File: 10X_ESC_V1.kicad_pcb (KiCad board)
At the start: 4 copper layers, 66 x 61.8 mm, 98 parts, among them J1 Conn_01x05_MountingPin, Q1 BUK7Y1R4-40H, Q2 BUK7Y1R4-40H, Q3 BUK7Y1R4-40H, Q4 BUK7Y1R4-40H, Q5 BUK7Y1R4-40H, Q7 BUK7Y1R4-40H, U1 STM32F051K8Ux, U2 DRV8300DPWR, U3 TPS62932, U4 TPS62932, U5 INA180B2

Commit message: D1~D3 부트스트랩 다이오드 제거 (DRV8300D 내장)
README에 있던 불필요한 다이오드 제거 완료
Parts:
- removed ?: , 
- removed D1, D2, D3: D, Diode_SMD:D_SMA
- removed REF**: Capacitor_Through_Hole, Footprints:Capacitor_Through_Hole
- TP6: value SWDIO -> TELEMRX
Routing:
- net +12V: track 74.0 -> 56.6 mm
- net Net-(U2-BSTC): track 6.15 -> 2.99 mm
- net Net-(U2-BSTB): track 5.42 -> 2.46 mm
- net Net-(U2-BSTA): track 5.25 -> 2.52 mm

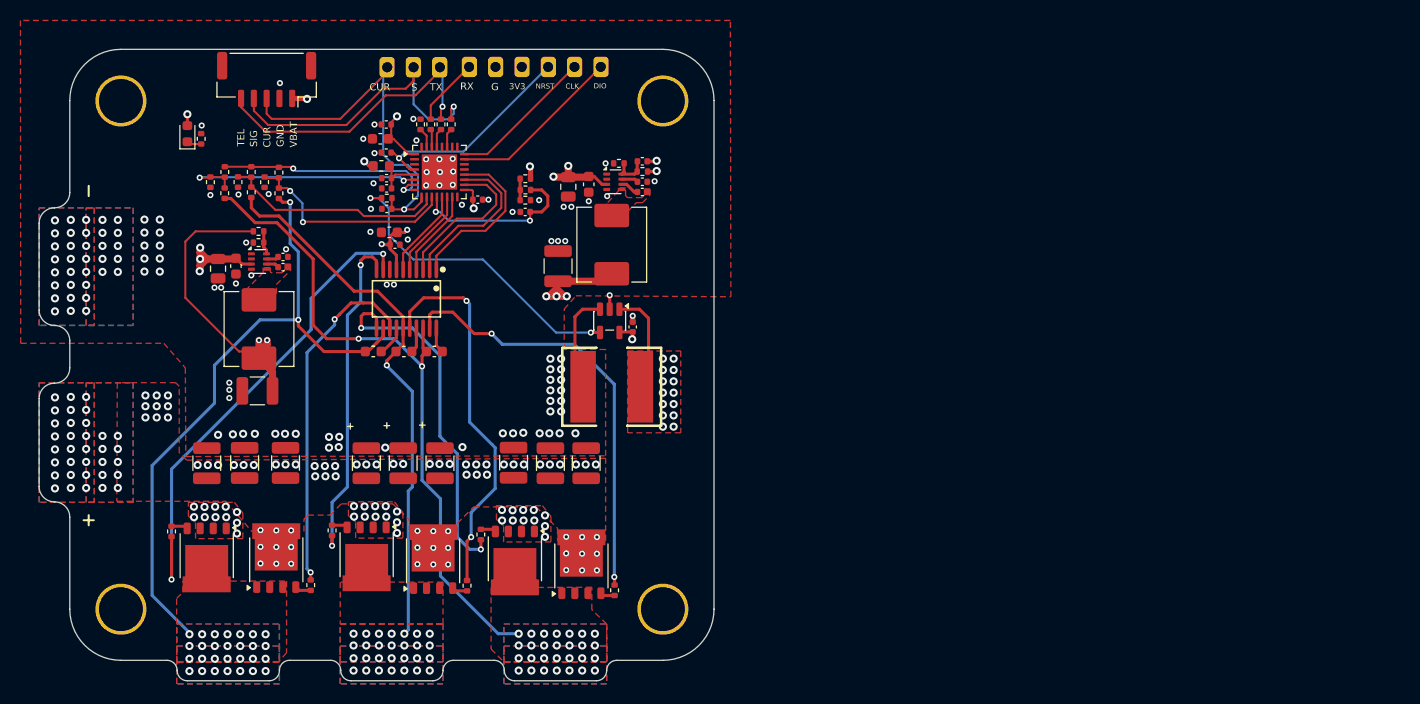
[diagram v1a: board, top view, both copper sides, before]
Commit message: V2 배치 연습
V2 배치 연습: 30x21 외곽선, MOSFET 아랫면 3열 배치
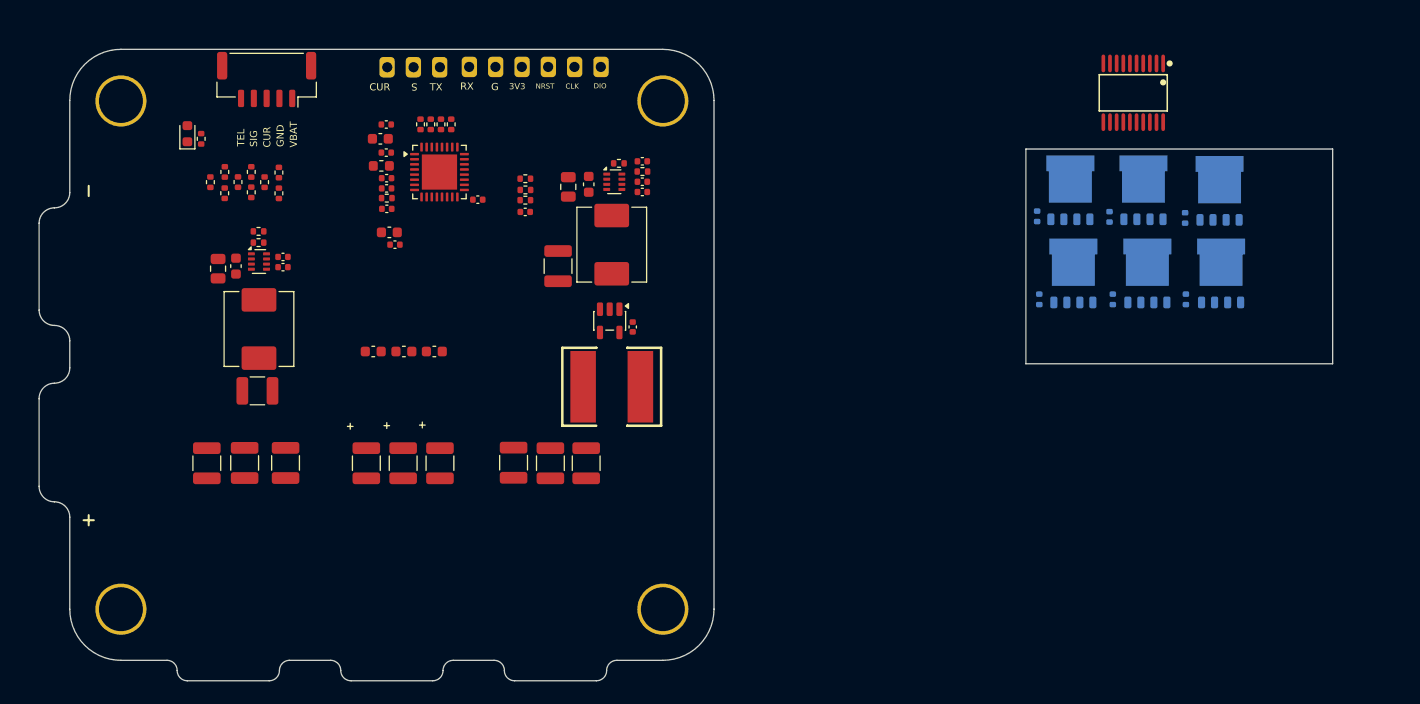
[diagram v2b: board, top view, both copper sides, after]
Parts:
- Q1, Q2, Q3, Q4, Q5, Q7, R10, R11, R6, R7, R8, R9: moved to B.Cu
- moved Q1 102.9 mm to (195.6, 99.3), turned to 90 degrees
- moved R7 101.8 mm to (192.2, 101.7), turned to -90 degrees
- moved Q7 99.0 mm to (195.4, 91.3)
- moved R6 92.7 mm to (192.1, 93.7)
- moved Q2 81.1 mm to (188.4, 99.3), turned to 90 degrees
- moved R8 79.6 mm to (185.0, 101.7), turned to -90 degrees
- moved Q3 78.3 mm to (188.0, 91.2)
- moved U2 73.9 mm to (187.0, 81.5)
- moved R9 72.4 mm to (184.7, 93.6)
- moved Q5 61.3 mm to (181.1, 99.3), turned to 90 degrees
- moved Q4 60.2 mm to (180.8, 91.2)
- moved R10 59.3 mm to (177.8, 101.7), turned to -90 degrees
- moved R11 55.2 mm to (177.6, 93.6)
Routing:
- net +BATT: track 90.3 -> 0.00 mm, vias 115 -> 0
- net GND: track 71.7 -> 0.00 mm, vias 125 -> 0
- net MOTORA: track 65.2 -> 0.00 mm, vias 30 -> 0
- net MOTORC: track 64.9 -> 0.00 mm, vias 30 -> 0
- net +12V: track 56.6 -> 0.00 mm, vias 4 -> 0
- net MOTORB: track 53.4 -> 0.00 mm, vias 29 -> 0
- net GLC: track 47.8 -> 0.00 mm, vias 2 -> 0
- net GHA: track 42.2 -> 0.00 mm, vias 2 -> 0
- net CURRENT: track 37.5 -> 0.00 mm, vias 1 -> 0
- net GHB: track 37.5 -> 0.00 mm, vias 2 -> 0
- net GLA: track 34.9 -> 0.00 mm, vias 2 -> 0
- net GHC: track 34.3 -> 0.00 mm, vias 2 -> 0
- net GLB: track 32.7 -> 0.00 mm, vias 2 -> 0
- net SIGNAL_INPUT: track 30.9 -> 0.00 mm, vias 1 -> 0
- net Net-(R24-Pad1): track 30.5 -> 0.00 mm, vias 2 -> 0
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- removed copper zone on In2.Cu, net +3.3V
- removed copper zone on B.Cu, net +BATT
- removed copper zone on F.Cu, net +BATT
- removed copper zone on In2.Cu, net +BATT
- removed copper zone on F.Cu, net /HALF BRIDGE GND
- removed copper zone on In1.Cu, net /HALF BRIDGE GND
- removed copper zone on In2.Cu, net /HALF BRIDGE GND
- removed copper zone on B.Cu, net GND
- removed copper zone on F.Cu, net GND
- removed copper zone on In1.Cu, net GND
- removed copper zone on B.Cu, net MOTORA
- removed copper zone on F.Cu, net MOTORA
- removed copper zone on B.Cu, net MOTORB
- removed copper zone on F.Cu, net MOTORB
- removed copper zone on B.Cu, net MOTORC
- removed copper zone on F.Cu, net MOTORC
- removed copper zone on F.Cu, net Net-(U3-SW)
- removed copper zone on F.Cu, net Net-(U4-SW)
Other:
- board size 66 x 61.8 mm -> 126.5 x 61.8 mm

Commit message: V2 배치 연습: MCU, 게이트 드라이버, 12V/3.3V 벅 배치 시도
30x21에 전원부가 다 안 들어감. 다음 단계에서 3.3V 벅 → LDO 교체 등 최적화 예정
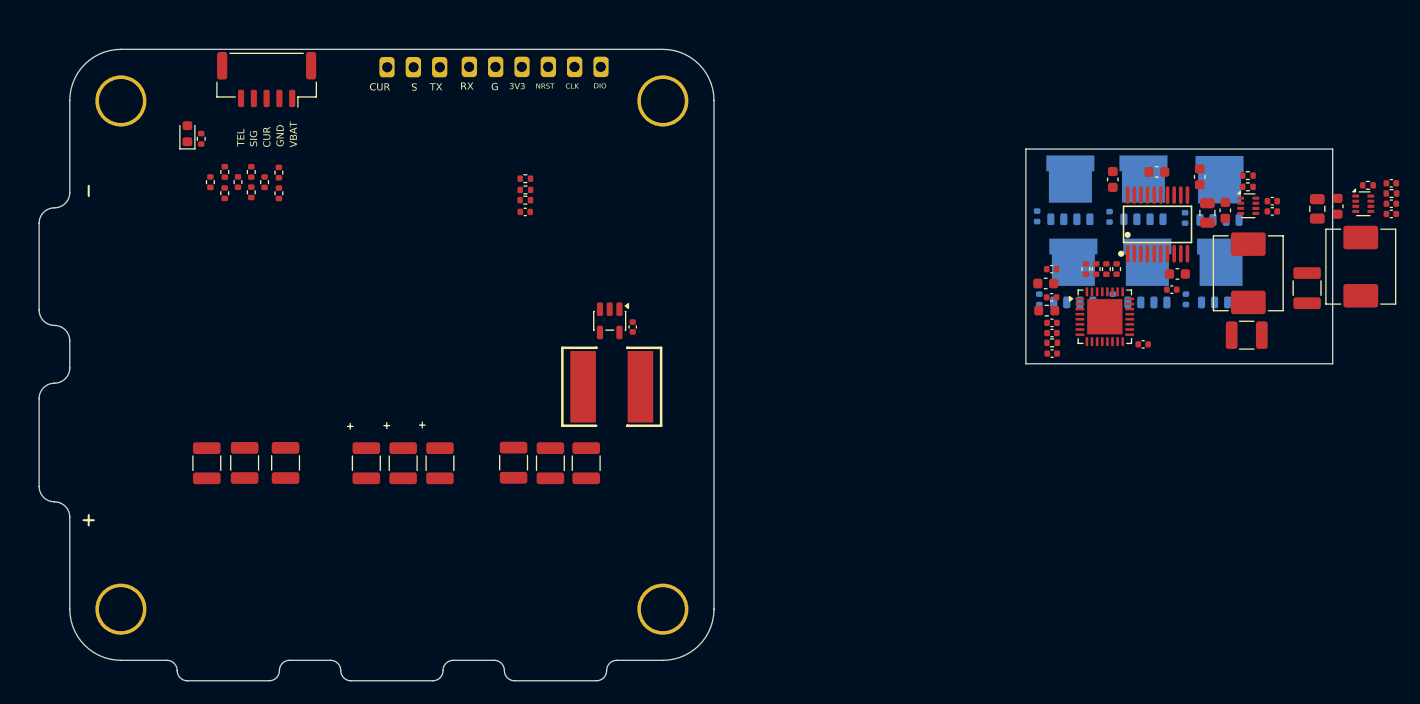
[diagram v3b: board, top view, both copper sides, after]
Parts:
- moved R25 96.9 mm to (198.2, 89.6)
- moved R26 96.9 mm to (198.2, 90.7)
- moved C25 96.9 mm to (194.2, 93.2)
- moved C26 96.9 mm to (196.0, 93.0)
- moved C27 96.9 mm to (200.6, 92.1)
- moved C30 96.9 mm to (200.6, 93.1)
- moved C32 96.9 mm to (198.1, 105.2)
- moved L2 96.9 mm to (198.2, 99.2)
- moved U4 96.9 mm to (198.2, 92.5)
- moved C18 82.6 mm to (193.5, 89.7), turned to 90 degrees
- moved C15 77.2 mm to (191.3, 99.2), turned to 180 degrees
- moved C14 76.1 mm to (190.8, 100.8), turned to 0 degrees
- moved C17 75.7 mm to (189.3, 89.2), turned to 180 degrees
- moved C19 73.3 mm to (205.0, 92.8)
- moved C20 73.3 mm to (207.0, 92.6)
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
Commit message: 3.3V 벅 → LDO(TPS70933DBVR) 교체 및 배치
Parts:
- removed C21: 33n, Capacitor_SMD:C_0402_1005Metric
- removed C22: 100n, Capacitor_SMD:C_0402_1005Metric
- removed C23: 15p, Capacitor_SMD:C_0402_1005Metric
- removed C24: 47u, Capacitor_SMD:C_1210_3225Metric
- removed L1: 8u2, Inductor_SMD:L_KOHERelec_MDA7030
- removed R3: 30k9, Resistor_SMD:R_0402_1005Metric
- removed R4: 10k, Resistor_SMD:R_0402_1005Metric
- C19: value 10u -> 1u; footprint Capacitor_SMD:C_0805_2012Metric -> Capacitor_SMD:C_0603_1608Metric
- C20: value 100n -> 2.2u
- U3: value TPS62932 -> TPS70933DBVR; footprint Package_TO_SOT_SMD:SOT-583-8 -> Package_TO_SOT_SMD:SOT-23-5
- moved U3 27.6 mm to (181.9, 93.1), turned to 90 degrees
- moved C20 26.3 mm to (180.9, 89.1), turned to 90 degrees
- moved C19 24.4 mm to (180.9, 96.9), turned to 90 degrees
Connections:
- C19 pad 1: +BATT -> +12V
- C20 pad 1: +BATT -> +3.3V
- U3 pad 1: unconnected-(U3-RT-Pad1) -> +12V
- U3 pad 2: unconnected-(U3-EN-Pad2) -> GND
- U3 pad 3: +BATT -> +12V
- U3 pad 4: GND -> unconnected-(U3-NC-Pad4)
- U3 pad 5: Net-(U3-SW) -> +3.3V

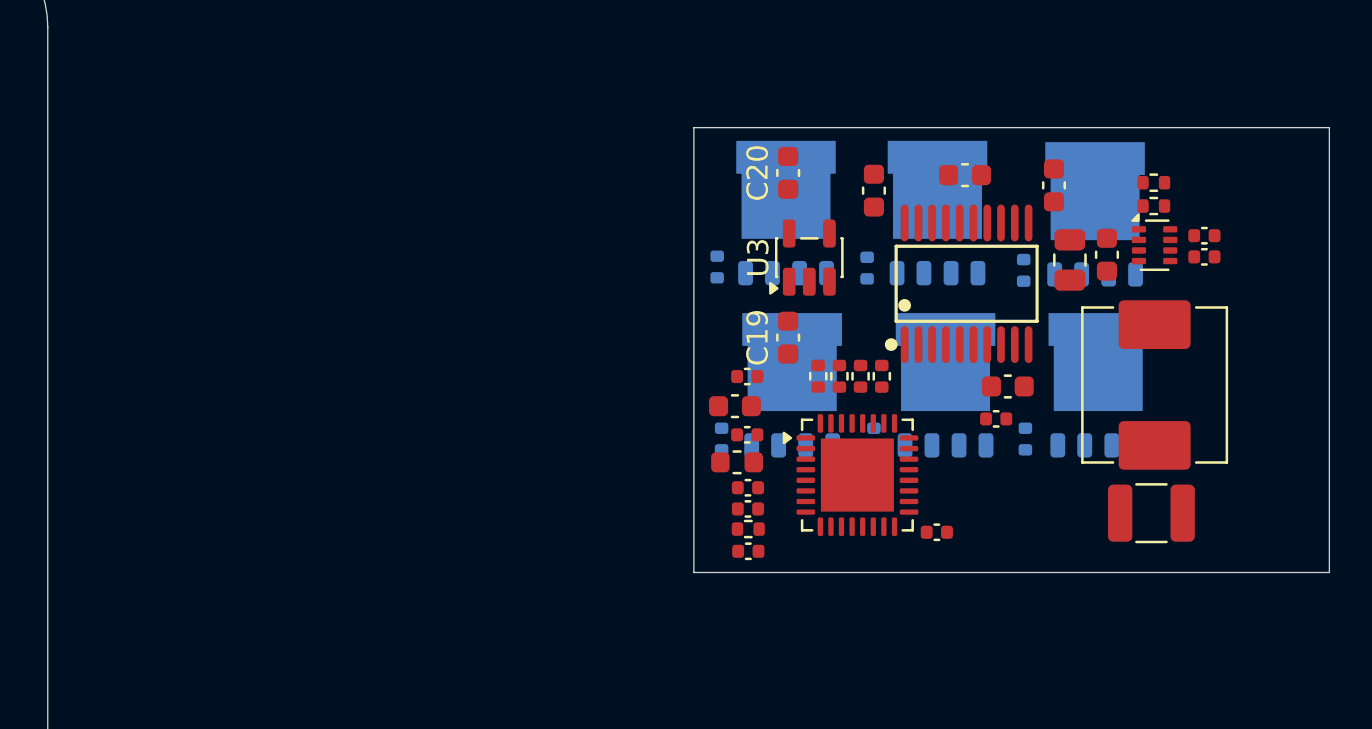
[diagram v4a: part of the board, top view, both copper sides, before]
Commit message: 전류 센서(U5, R12) 삭제, 로우사이드 소스 GND 직결
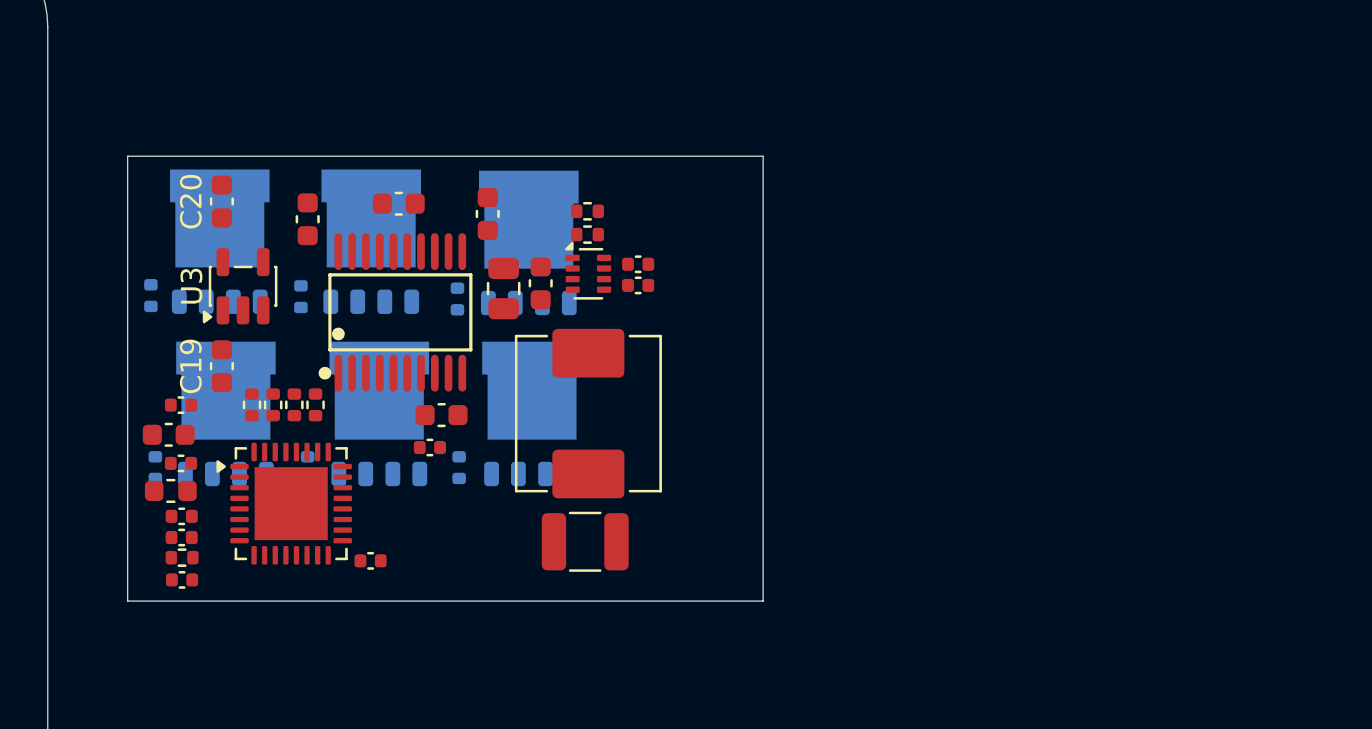
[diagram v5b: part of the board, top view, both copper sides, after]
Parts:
- moved C1 26.8 mm to (152.3, 100.1)
- moved C14 26.8 mm to (164.0, 102.1)
- moved C17 26.8 mm to (162.6, 90.6)
- moved C4 26.8 mm to (152.3, 102.8)
- moved C5 26.8 mm to (152.3, 106.3)
- moved C6 26.8 mm to (152.3, 105.3)
- moved R1 26.8 mm to (155.6, 100.1)
- moved R2 26.8 mm to (158.6, 100.1)
- moved R25 26.8 mm to (171.5, 91.0)
- moved R26 26.8 mm to (171.5, 92.0)
- moved R28 26.8 mm to (157.6, 100.1)
- moved R29 26.8 mm to (156.6, 100.1)
- moved R7 26.8 mm to (165.4, 103.0)
- moved R9 26.8 mm to (157.9, 95.0)
- moved C15 26.8 mm to (164.6, 100.6)
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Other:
- board size 126.5 x 61.8 mm -> 99.8 x 61.8 mm

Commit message: 개발 보드 요소 삭제 (장착구멍, LED, 테스트포인트), SWD 패드 4개로 축소
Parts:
- removed C28, C29: 100n, Capacitor_SMD:C_0402_1005Metric
- removed D4: LED, LED_SMD:LED_0603_1608Metric
- removed H1, H2, H3, H4: MountingHole_Pad, Footprints:Flightcontroller_MountingHolePad_M4
- removed R12: 1m, Footprints:R2725
- removed R24: 1k, Resistor_SMD:R_0402_1005Metric
- removed R5: 1k5, Resistor_SMD:R_0402_1005Metric
- removed TP3: NRST, Footprints:Flightcontroller_Solder_Pad
- removed TP6: TELEMRX, Footprints:Flightcontroller_Solder_Pad
- removed TP7: CURRENT, Footprints:Flightcontroller_Solder_Pad
- removed TP8: SIGNAL_INPUT, Footprints:Flightcontroller_Solder_Pad
- removed TP9: TELEMETRY, Footprints:Flightcontroller_Solder_Pad
- removed U5: INA180B2, Package_TO_SOT_SMD:SOT-23-5
- TP1, TP2, TP4, TP5: footprint Footprints:Flightcontroller_Solder_Pad -> TestPoint:TestPoint_Pad_D1.0mm
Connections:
- Q1 pad 1: /HALF BRIDGE GND -> GND
- Q1 pad 2: /HALF BRIDGE GND -> GND
- Q1 pad 3: /HALF BRIDGE GND -> GND
- Q2 pad 1: /HALF BRIDGE GND -> GND
- Q2 pad 2: /HALF BRIDGE GND -> GND
- Q2 pad 3: /HALF BRIDGE GND -> GND
- Q5 pad 1: /HALF BRIDGE GND -> GND
- Q5 pad 2: /HALF BRIDGE GND -> GND
- Q5 pad 3: /HALF BRIDGE GND -> GND
- U1 pad 9: CURRENT -> unconnected-(U1-PA3-Pad9)
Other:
- board text removed: "NRST"
- board text removed: "RX"
- board text removed: "S"
- board text removed: "TX"
